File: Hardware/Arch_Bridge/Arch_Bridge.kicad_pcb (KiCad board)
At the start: 2 copper layers, 88.8 x 76 mm, 87 parts, among them J1 Conn_01x02, J3 Conn_01x04, J4 Conn_01x04, Q1 2N3904, Q2 MJE2955, Q3 MJE2955, U1 AP63205WU, U10 74AHC1G04, U11 ESP32-S3-WROOM-1, U12 TXS0102DCT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

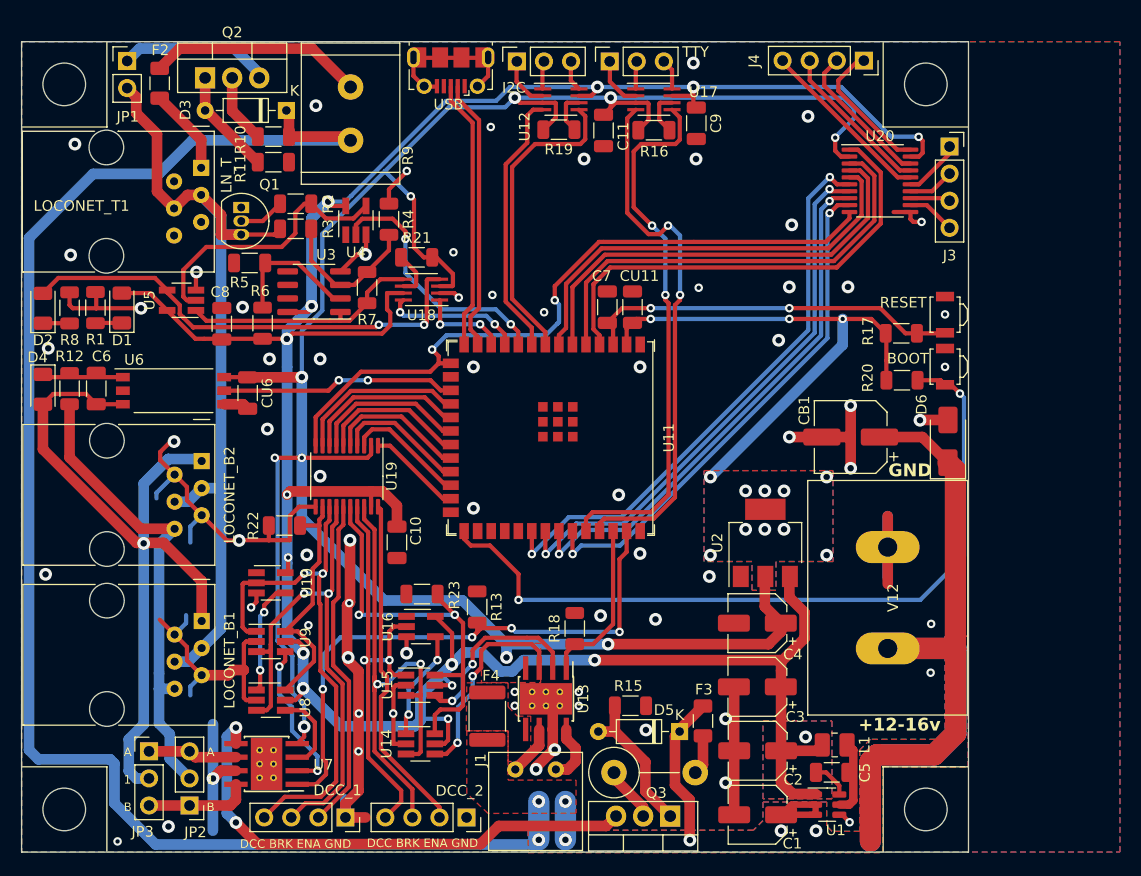
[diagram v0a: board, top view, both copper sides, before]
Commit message: Completed BOM, PCB layout cleanup, starting software.
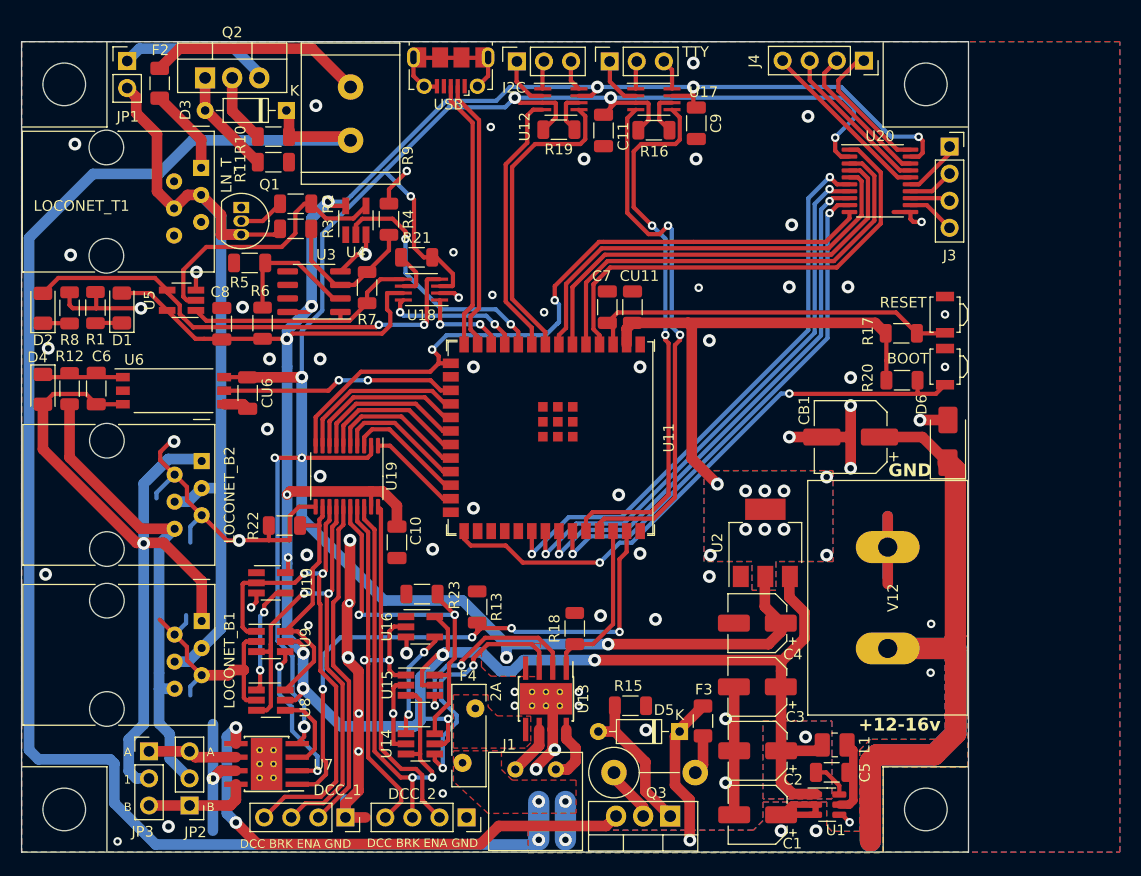
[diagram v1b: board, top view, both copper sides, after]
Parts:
- F4: footprint Fuse:Fuse_1812_4532Metric_Pad1.30x3.40mm_HandSolder -> Fuse:Fuse_Bourns_MF-RHT200
- U10, U16, U4: value 74AHC1G04 -> 74LVC1G04
- U3: value LM393 -> LM393B
- U5: value 74AHCT1G02 -> 74LVC1G02
- moved F4 4.95 mm to (61.4, 87.6)
- moved U16 0.06 mm to (57.4, 74.9)
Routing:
- net Net-(U11-GPIO0/BOOT): track 73.0 -> 55.0 mm
- net /BRK_2: track 48.4 -> 44.1 mm
- net Net-(U13-IN1): track 19.7 -> 23.8 mm
- net +3.3V: track 274.1 -> 270.3 mm, vias 23 -> 20
- net /ENA_2o: track 38.4 -> 35.5 mm
- net +5V: track 271.4 -> 273.6 mm, vias 15 -> 14
- net Net-(U13-IN2): track 17.1 -> 18.4 mm
- net /RESET: track 35.5 -> 35.2 mm, vias 2 -> 0
- net GND: vias 70 -> 73
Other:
- board text added: "Arch Bridge Loconet interface + Railsync"
- board text added: "Seraphimlabs LLC 2023 github.com/SeraphimlabsLLC"

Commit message: Revised L1 for possible 2A output, cleaner fill zones, fabrication outputs
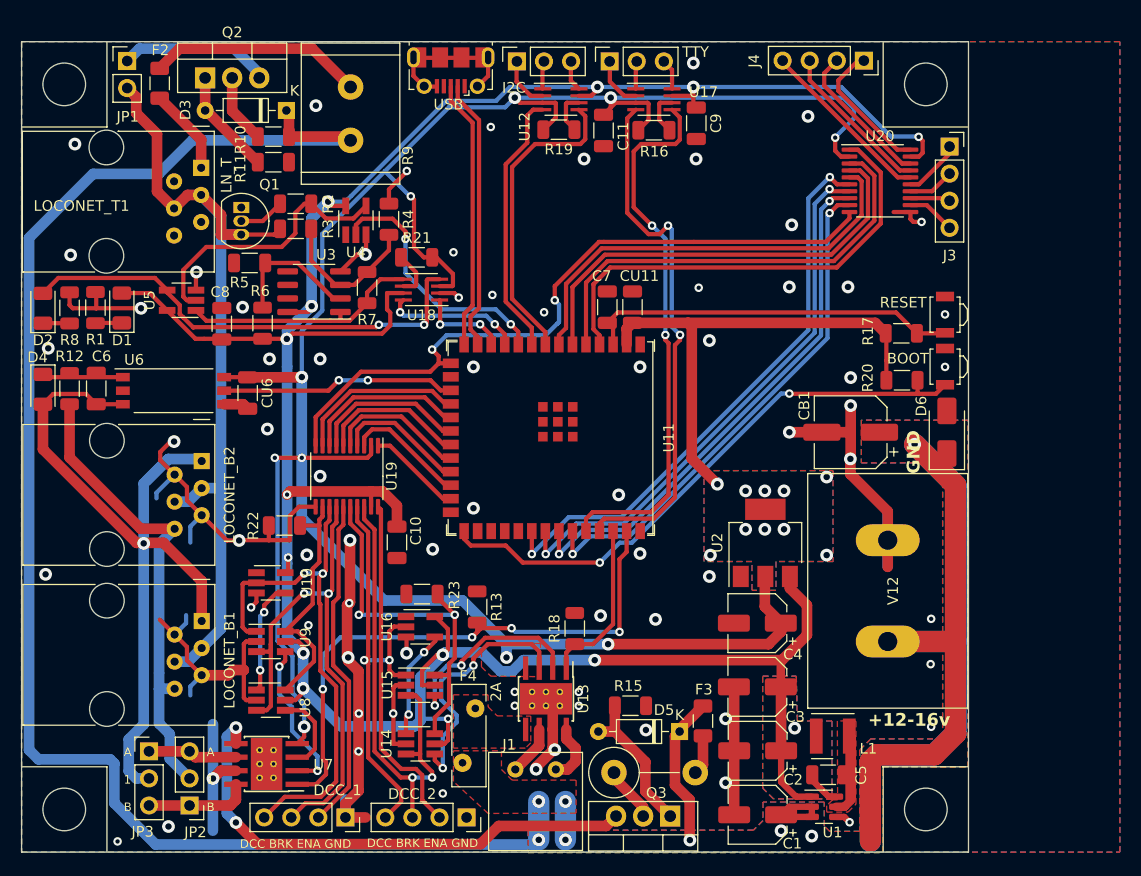
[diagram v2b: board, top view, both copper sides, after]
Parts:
- L1: footprint Inductor_SMD:L_1008_2520Metric_Pad1.43x2.20mm_HandSolder -> Inductor_SMD_Wurth:L_Wurth_WE-LQSH-4020
- moved D6 0.86 mm to (106.8, 56.6)
- moved L1 0.84 mm to (96.1, 85.1)
- moved V12 0.65 mm to (101.2, 71.5)
- moved CB1 0.45 mm to (97.8, 56.6)
- moved C5 0.42 mm to (95.6, 88.8)
- moved U1 0.36 mm to (95.2, 91.8)
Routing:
- net +12V: track 260.5 -> 276.2 mm, vias 7 -> 8
- net +5V: track 273.6 -> 269.5 mm
- net GND: track 207.4 -> 208.7 mm
- net Net-(U1-SW): track 6.91 -> 7.55 mm
- added copper zone on F.Cu, net Net-(U1-SW)
